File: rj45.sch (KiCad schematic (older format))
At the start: 0 parts

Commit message: Added isolators and RJ-45 connectors
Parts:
- added Jx: RJ45, symbol Connector:RJ45
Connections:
- net labels added: GNDREF, OUT1, OUT2, OUT3, OUT4
- wire segments 0 -> 12
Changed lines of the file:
@@
 $Descr A4 11693 8268
 encoding utf-8
-Sheet 5 5
+Sheet 8 8
 Title ""
 Date ""
@@
 Comment4 ""
 $EndDescr
+$Comp
+L Connector:RJ45 Jx
+U 1 1 5BCCA258
+P 6050 4100
+F 0 "Jx" H 5720 4196 50  0000 R CNN
+F 1 "RJ45" H 5720 4105 50  0000 R CNN
+F 2 "" V 6050 4125 50  0001 C CNN
+F 3 "~" V 6050 4125 50  0001 C CNN
+	1    6050 4100
+	-1   0    0    -1
+$EndComp
+$Comp
+L power:GNDREF #PWR?
+U 1 1 5BCCA2D6
+P 5450 4600
+F 0 "#PWR?" H 5450 4350 50  0001 C CNN
+F 1 "GNDREF" H 5455 4427 50  0000 C CNN
+F 2 "" H 5450 4600 50  0001 C CNN
+F 3 "" H 5450 4600 50  0001 C CNN
+	1    5450 4600
+	1    0    0    -1
+$EndComp
+Wire Wire Line
+	5450 4600 5450 4400
+Wire Wire Line
+	5450 3800 5650 3800
+Wire Wire Line
+	5650 4000 5450 4000
+Connection ~ 5450 4000
+Wire Wire Line
+	5450 4000 5450 3800
+Wire Wire Line
+	5650 4200 5450 4200
+Connection ~ 5450 4200
+Wire Wire Line
+	5450 4200 5450 4000
+Wire Wire Line
+	5650 4400 5450 4400
+Connection ~ 5450 4400
+Wire Wire Line
+	5450 4400 5450 4200
+Text HLabel 5200 3700 0    50   Input ~ 0
+OUT1
+Text HLabel 5200 3900 0    50   Input ~ 0
+OUT2
+Text HLabel 5200 4100 0    50   Input ~ 0
+OUT3
+Text HLabel 5200 4300 0    50   Input ~ 0
+OUT4
+Wire Wire Line
+	5200 4300 5650 4300
+Wire Wire Line
+	5200 4100 5650 4100
+Wire Wire Line
+	5200 3900 5650 3900
+Wire Wire Line
+	5200 3700 5650 3700
 $EndSCHEMATC

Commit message: Added charge pump IC REG71050
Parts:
- renumbered Jx to Jx1
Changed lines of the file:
@@
 $Descr A4 11693 8268
 encoding utf-8
-Sheet 8 8
+Sheet 8 11
 Title ""
 Date ""
@@
 $EndDescr
 $Comp
-L Connector:RJ45 Jx
+L Connector:RJ45 Jx1
 U 1 1 5BCCA258
 P 6050 4100
-F 0 "Jx" H 5720 4196 50  0000 R CNN
+AR Path="/5BCCA241/5BCCA258" Ref="Jx1"  Part="1"
+AR Path="/5BCCB065/5BCCA258" Ref="Jx2"  Part="1"
+AR Path="/5BCCB3D0/5BCCA258" Ref="Jx3"  Part="1"
+AR Path="/5BCCB87F/5BCCA258" Ref="Jx4"  Part="1"
+F 0 "Jx1" H 5720 4196 50  0000 R CNN
 F 1 "RJ45" H 5720 4105 50  0000 R CNN
 F 2 "" V 6050 4125 50  0001 C CNN
@@
 $EndComp
 $Comp
-L power:GNDREF #PWR?
+L power:GNDREF #PWR0126
 U 1 1 5BCCA2D6
 P 5450 4600
-F 0 "#PWR?" H 5450 4350 50  0001 C CNN
+AR Path="/5BCCA241/5BCCA2D6" Ref="#PWR0126"  Part="1"
+AR Path="/5BCCB065/5BCCA2D6" Ref="#PWR0127"  Part="1"
+AR Path="/5BCCB3D0/5BCCA2D6" Ref="#PWR0128"  Part="1"
+AR Path="/5BCCB87F/5BCCA2D6" Ref="#PWR0129"  Part="1"
+F 0 "#PWR0126" H 5450 4350 50  0001 C CNN
 F 1 "GNDREF" H 5455 4427 50  0000 C CNN
 F 2 "" H 5450 4600 50  0001 C CNN

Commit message: Assigned footprints
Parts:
- Jx1: footprint (none) -> Connector_RJ:RJ45_Amphenol_54602-x08_Horizontal
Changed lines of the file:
@@
 F 0 "Jx1" H 5720 4196 50  0000 R CNN
 F 1 "RJ45" H 5720 4105 50  0000 R CNN
-F 2 "" V 6050 4125 50  0001 C CNN
+F 2 "Connector_RJ:RJ45_Amphenol_54602-x08_Horizontal" V 6050 4125 50  0001 C CNN
 F 3 "~" V 6050 4125 50  0001 C CNN
 	1    6050 4100

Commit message: Continued layouting
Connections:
- net labels added: GND
- net labels removed: GNDREF
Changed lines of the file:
@@
 AR Path="/5BCCB3D0/5BCCA258" Ref="Jx3"  Part="1"
 AR Path="/5BCCB87F/5BCCA258" Ref="Jx4"  Part="1"
-F 0 "Jx1" H 5720 4196 50  0000 R CNN
+F 0 "Jx4" H 5720 4196 50  0000 R CNN
 F 1 "RJ45" H 5720 4105 50  0000 R CNN
 F 2 "Connector_RJ:RJ45_Amphenol_54602-x08_Horizontal" V 6050 4125 50  0001 C CNN
@@
 	1    6050 4100
 	-1   0    0    -1
-$EndComp
-$Comp
-L power:GNDREF #PWR0126
-U 1 1 5BCCA2D6
-P 5450 4600
-AR Path="/5BCCA241/5BCCA2D6" Ref="#PWR0126"  Part="1"
-AR Path="/5BCCB065/5BCCA2D6" Ref="#PWR0127"  Part="1"
-AR Path="/5BCCB3D0/5BCCA2D6" Ref="#PWR0128"  Part="1"
-AR Path="/5BCCB87F/5BCCA2D6" Ref="#PWR0129"  Part="1"
-F 0 "#PWR0126" H 5450 4350 50  0001 C CNN
-F 1 "GNDREF" H 5455 4427 50  0000 C CNN
-F 2 "" H 5450 4600 50  0001 C CNN
-F 3 "" H 5450 4600 50  0001 C CNN
-	1    5450 4600
-	1    0    0    -1
 $EndComp
 Wire Wire Line
@@
 Wire Wire Line
 	5200 3700 5650 3700
+$Comp
+L power:GND #PWR042
+U 1 1 5BCF77E9
+P 5450 4600
+AR Path="/5BCCA241/5BCF77E9" Ref="#PWR042"  Part="1"
+AR Path="/5BCCB065/5BCF77E9" Ref="#PWR043"  Part="1"
+AR Path="/5BCCB3D0/5BCF77E9" Ref="#PWR044"  Part="1"
+AR Path="/5BCCB87F/5BCF77E9" Ref="#PWR045"  Part="1"
+F 0 "#PWR045" H 5450 4350 50  0001 C CNN
+F 1 "GND" H 5455 4427 50  0000 C CNN
+F 2 "" H 5450 4600 50  0001 C CNN
+F 3 "" H 5450 4600 50  0001 C CNN
+	1    5450 4600
+	1    0    0    -1
+$EndComp
 $EndSCHEMATC

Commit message: Switched to Si8660 isolator and changed RJ-45 connector
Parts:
- removed Jx1: RJ45, Connector_RJ:RJ45_Amphenol_54602-x08_Horizontal, symbol Connector:RJ45
- added J3: TE-Connectivity-406549-6, Matthias:TE-Connectivity-406549-6, symbol Matthias:TE-Connectivity-406549-6
- added R1, R2: R_Small, symbol Device:R_Small
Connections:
- net labels added: LED1, LED2
- wire segments 12 -> 23
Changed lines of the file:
@@
 $Descr A4 11693 8268
 encoding utf-8
-Sheet 8 11
+Sheet 10 11
 Title ""
 Date ""
@@
 Comment4 ""
 $EndDescr
+Wire Wire Line
+	6900 3800 6700 3800
+Wire Wire Line
+	6700 4000 6900 4000
+Connection ~ 6900 4000
+Wire Wire Line
+	6900 4000 6900 3800
+Wire Wire Line
+	6700 4200 6900 4200
+Connection ~ 6900 4200
+Wire Wire Line
+	6900 4200 6900 4000
+Wire Wire Line
+	6700 4400 6900 4400
+Connection ~ 6900 4400
+Wire Wire Line
+	6900 4400 6900 4200
+Text HLabel 7150 3700 2    50   Input ~ 0
+OUT1
+Text HLabel 7150 3900 2    50   Input ~ 0
+OUT2
+Text HLabel 7150 4100 2    50   Input ~ 0
+OUT3
+Text HLabel 7150 4300 2    50   Input ~ 0
+OUT4
+Wire Wire Line
+	7150 4300 6700 4300
+Wire Wire Line
+	7150 4100 6700 4100
+Wire Wire Line
+	7150 3900 6700 3900
+Wire Wire Line
+	7150 3700 6700 3700
 $Comp
-L Connector:RJ45 Jx1
-U 1 1 5BCCA258
-P 6050 4100
-AR Path="/5BCCA241/5BCCA258" Ref="Jx1"  Part="1"
-AR Path="/5BCCB065/5BCCA258" Ref="Jx2"  Part="1"
-AR Path="/5BCCB3D0/5BCCA258" Ref="Jx3"  Part="1"
-AR Path="/5BCCB87F/5BCCA258" Ref="Jx4"  Part="1"
-F 0 "Jx4" H 5720 4196 50  0000 R CNN
-F 1 "RJ45" H 5720 4105 50  0000 R CNN
-F 2 "Connector_RJ:RJ45_Amphenol_54602-x08_Horizontal" V 6050 4125 50  0001 C CNN
-F 3 "~" V 6050 4125 50  0001 C CNN
-	1    6050 4100
-	-1   0    0    -1
+L power:GND #PWR044
+U 1 1 5BCF77E9
+P 6900 4950
+AR Path="/5BCCA241/5BCF77E9" Ref="#PWR044"  Part="1"
+AR Path="/5BCCB065/5BCF77E9" Ref="#PWR047"  Part="1"
+AR Path="/5BCCB3D0/5BCF77E9" Ref="#PWR050"  Part="1"
+AR Path="/5BCCB87F/5BCF77E9" Ref="#PWR053"  Part="1"
+F 0 "#PWR053" H 6900 4700 50  0001 C CNN
+F 1 "GND" H 6905 4777 50  0000 C CNN
+F 2 "" H 6900 4950 50  0001 C CNN
+F 3 "" H 6900 4950 50  0001 C CNN
+	1    6900 4950
+	1    0    0    -1
+$EndComp
+$Comp
+L Matthias:TE-Connectivity-406549-6 J3
+U 1 1 5BE0C1CD
+P 6300 4100
+AR Path="/5BCCA241/5BE0C1CD" Ref="J3"  Part="1"
+AR Path="/5BCCB3D0/5BE0C1CD" Ref="J5"  Part="1"
+AR Path="/5BCCB065/5BE0C1CD" Ref="J4"  Part="1"
+AR Path="/5BCCB87F/5BE0C1CD" Ref="J6"  Part="1"
+F 0 "J6" H 6300 4775 50  0000 C CNN
+F 1 "TE-Connectivity-406549-6" H 6300 4684 50  0000 C CNN
+F 2 "Matthias:TE-Connectivity-406549-6" V 6300 4125 50  0001 C CNN
+F 3 "~" V 6300 4125 50  0001 C CNN
+	1    6300 4100
+	1    0    0    -1
+$EndComp
+Text HLabel 5550 3750 0    50   Input ~ 0
+LED1
+Text HLabel 5550 4450 0    50   Input ~ 0
+LED2
+Wire Wire Line
+	6900 4400 6900 4750
+Wire Wire Line
+	6250 4650 6250 4750
+Wire Wire Line
+	6250 4750 6400 4750
+Connection ~ 6900 4750
+Wire Wire Line
+	6900 4750 6900 4950
+Wire Wire Line
+	6400 4650 6400 4750
+Connection ~ 6400 4750
+Wire Wire Line
+	6400 4750 6900 4750
+Wire Wire Line
+	5900 4450 5550 4450
+Wire Wire Line
+	5900 3750 5550 3750
+$Comp
+L Device:R_Small R1
+U 1 1 5BE0DDBF
+P 5100 3650
+AR Path="/5BCCA241/5BE0DDBF" Ref="R1"  Part="1"
+AR Path="/5BCCB3D0/5BE0DDBF" Ref="R5"  Part="1"
+AR Path="/5BCCB065/5BE0DDBF" Ref="R3"  Part="1"
+AR Path="/5BCCB87F/5BE0DDBF" Ref="R7"  Part="1"
+F 0 "R7" V 4904 3650 50  0000 C CNN
+F 1 "R_Small" V 4995 3650 50  0000 C CNN
+F 2 "" H 5100 3650 50  0001 C CNN
+F 3 "~" H 5100 3650 50  0001 C CNN
+	1    5100 3650
+	0    1    1    0
 $EndComp
 Wire Wire Line
-	5450 4600 5450 4400
-Wire Wire Line
-	5450 3800 5650 3800
-Wire Wire Line
-	5650 4000 5450 4000
-Connection ~ 5450 4000
-Wire Wire Line
-	5450 4000 5450 3800
-Wire Wire Line
-	5650 4200 5450 4200
-Connection ~ 5450 4200
-Wire Wire Line
-	5450 4200 5450 4000
-Wire Wire Line
-	5650 4400 5450 4400
-Connection ~ 5450 4400
-Wire Wire Line
-	5450 4400 5450 4200
-Text HLabel 5200 3700 0    50   Input ~ 0
-OUT1
-Text HLabel 5200 3900 0    50   Input ~ 0
-OUT2
-Text HLabel 5200 4100 0    50   Input ~ 0
-OUT3
-Text HLabel 5200 4300 0    50   Input ~ 0
-OUT4
-Wire Wire Line
-	5200 4300 5650 4300
-Wire Wire Line
-	5200 4100 5650 4100
-Wire Wire Line
-	5200 3900 5650 3900
-Wire Wire Line
-	5200 3700 5650 3700
+	5200 3650 5900 3650
 $Comp
 L power:GND #PWR042
-U 1 1 5BCF77E9
-P 5450 4600
-AR Path="/5BCCA241/5BCF77E9" Ref="#PWR042"  Part="1"
-AR Path="/5BCCB065/5BCF77E9" Ref="#PWR043"  Part="1"
-AR Path="/5BCCB3D0/5BCF77E9" Ref="#PWR044"  Part="1"
-AR Path="/5BCCB87F/5BCF77E9" Ref="#PWR045"  Part="1"
-F 0 "#PWR045" H 5450 4350 50  0001 C CNN
-F 1 "GND" H 5455 4427 50  0000 C CNN
-F 2 "" H 5450 4600 50  0001 C CNN
-F 3 "" H 5450 4600 50  0001 C CNN
-	1    5450 4600
+U 1 1 5BE0E201
+P 5000 3800
+AR Path="/5BCCA241/5BE0E201" Ref="#PWR042"  Part="1"
+AR Path="/5BCCB065/5BE0E201" Ref="#PWR045"  Part="1"
+AR Path="/5BCCB3D0/5BE0E201" Ref="#PWR048"  Part="1"
+AR Path="/5BCCB87F/5BE0E201" Ref="#PWR051"  Part="1"
+F 0 "#PWR051" H 5000 3550 50  0001 C CNN
+F 1 "GND" H 5005 3627 50  0000 C CNN
+F 2 "" H 5000 3800 50  0001 C CNN
+F 3 "" H 5000 3800 50  0001 C CNN
+	1    5000 3800
 	1    0    0    -1
 $EndComp
+Wire Wire Line
+	5000 3800 5000 3650
+$Comp
+L Device:R_Small R2
+U 1 1 5BE0E685
+P 5100 4350
+AR Path="/5BCCA241/5BE0E685" Ref="R2"  Part="1"
+AR Path="/5BCCB3D0/5BE0E685" Ref="R6"  Part="1"
+AR Path="/5BCCB065/5BE0E685" Ref="R4"  Part="1"
+AR Path="/5BCCB87F/5BE0E685" Ref="R8"  Part="1"
+F 0 "R8" V 4904 4350 50  0000 C CNN
+F 1 "R_Small" V 4995 4350 50  0000 C CNN
+F 2 "" H 5100 4350 50  0001 C CNN
+F 3 "~" H 5100 4350 50  0001 C CNN
+	1    5100 4350
+	0    1    1    0
+$EndComp
+Wire Wire Line
+	5200 4350 5900 4350
+$Comp
+L power:GND #PWR043
+U 1 1 5BE0E68D
+P 5000 4500
+AR Path="/5BCCA241/5BE0E68D" Ref="#PWR043"  Part="1"
+AR Path="/5BCCB065/5BE0E68D" Ref="#PWR046"  Part="1"
+AR Path="/5BCCB3D0/5BE0E68D" Ref="#PWR049"  Part="1"
+AR Path="/5BCCB87F/5BE0E68D" Ref="#PWR052"  Part="1"
+F 0 "#PWR052" H 5000 4250 50  0001 C CNN
+F 1 "GND" H 5005 4327 50  0000 C CNN
+F 2 "" H 5000 4500 50  0001 C CNN
+F 3 "" H 5000 4500 50  0001 C CNN
+	1    5000 4500
+	1    0    0    -1
+$EndComp
+Wire Wire Line
+	5000 4500 5000 4350
 $EndSCHEMATC

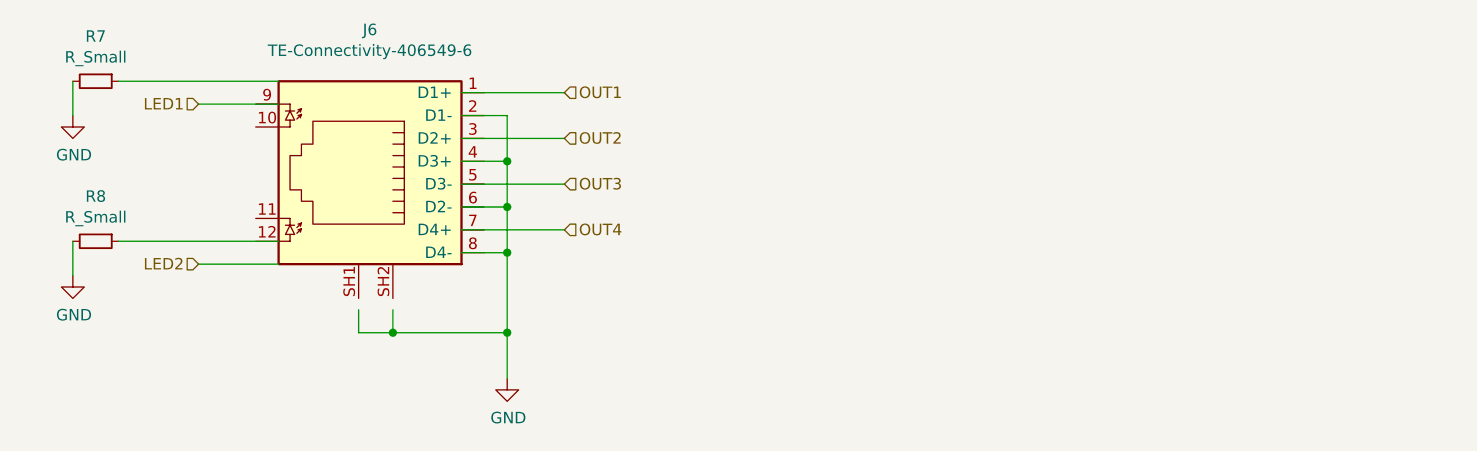
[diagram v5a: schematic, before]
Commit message: Updated RJ45 symbol and corresponding signal names
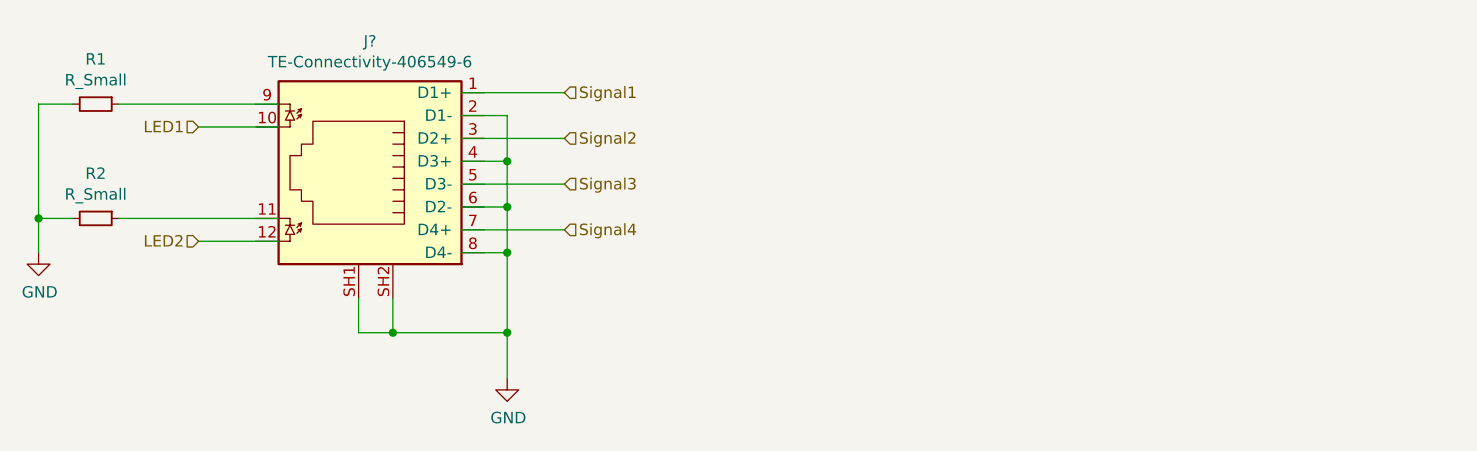
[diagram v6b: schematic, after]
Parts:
- removed J3: TE-Connectivity-406549-6, Matthias:TE-Connectivity-406549-6, symbol Matthias:TE-Connectivity-406549-6
- added J?: TE-Connectivity-406549-6, symbol Matthias:TE-Connectivity-406549-6
- R1, R2: footprint (none) -> Resistor_SMD:R_0805_2012Metric_Pad1.15x1.40mm_HandSolder
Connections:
- net labels added: Signal1, Signal2, Signal3, Signal4
- net labels removed: OUT1, OUT2, OUT3, OUT4
- wire segments 23 -> 25
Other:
- moved on the sheet: R1, R2
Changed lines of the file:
@@
 $Descr A4 11693 8268
 encoding utf-8
-Sheet 10 11
+Sheet 8 11
 Title ""
 Date ""
@@
 	6900 4400 6900 4200
 Text HLabel 7150 3700 2    50   Input ~ 0
-OUT1
+Signal1
 Text HLabel 7150 3900 2    50   Input ~ 0
-OUT2
+Signal2
 Text HLabel 7150 4100 2    50   Input ~ 0
-OUT3
+Signal3
 Text HLabel 7150 4300 2    50   Input ~ 0
-OUT4
+Signal4
 Wire Wire Line
 	7150 4300 6700 4300
@@
 AR Path="/5BCCB3D0/5BCF77E9" Ref="#PWR050"  Part="1"
 AR Path="/5BCCB87F/5BCF77E9" Ref="#PWR053"  Part="1"
-F 0 "#PWR053" H 6900 4700 50  0001 C CNN
+F 0 "#PWR044" H 6900 4700 50  0001 C CNN
 F 1 "GND" H 6905 4777 50  0000 C CNN
 F 2 "" H 6900 4950 50  0001 C CNN
@@
 	1    0    0    -1
 $EndComp
-$Comp
-L Matthias:TE-Connectivity-406549-6 J3
-U 1 1 5BE0C1CD
-P 6300 4100
-AR Path="/5BCCA241/5BE0C1CD" Ref="J3"  Part="1"
-AR Path="/5BCCB3D0/5BE0C1CD" Ref="J5"  Part="1"
-AR Path="/5BCCB065/5BE0C1CD" Ref="J4"  Part="1"
-AR Path="/5BCCB87F/5BE0C1CD" Ref="J6"  Part="1"
-F 0 "J6" H 6300 4775 50  0000 C CNN
-F 1 "TE-Connectivity-406549-6" H 6300 4684 50  0000 C CNN
-F 2 "Matthias:TE-Connectivity-406549-6" V 6300 4125 50  0001 C CNN
-F 3 "~" V 6300 4125 50  0001 C CNN
-	1    6300 4100
-	1    0    0    -1
-$EndComp
-Text HLabel 5550 3750 0    50   Input ~ 0
+Text HLabel 5550 3850 0    50   Input ~ 0
 LED1
-Text HLabel 5550 4450 0    50   Input ~ 0
+Text HLabel 5550 4350 0    50   Input ~ 0
 LED2
 Wire Wire Line
 	6900 4400 6900 4750
 Wire Wire Line
-	6250 4650 6250 4750
+	6250 4600 6250 4750
 Wire Wire Line
 	6250 4750 6400 4750
@@
 	6900 4750 6900 4950
 Wire Wire Line
-	6400 4650 6400 4750
+	6400 4600 6400 4750
 Connection ~ 6400 4750
 Wire Wire Line
 	6400 4750 6900 4750
 Wire Wire Line
-	5900 4450 5550 4450
+	5900 4350 5550 4350
 Wire Wire Line
-	5900 3750 5550 3750
+	5900 3850 5550 3850
 $Comp
 L Device:R_Small R1
 U 1 1 5BE0DDBF
-P 5100 3650
+P 5100 3750
 AR Path="/5BCCA241/5BE0DDBF" Ref="R1"  Part="1"
 AR Path="/5BCCB3D0/5BE0DDBF" Ref="R5"  Part="1"
 AR Path="/5BCCB065/5BE0DDBF" Ref="R3"  Part="1"
 AR Path="/5BCCB87F/5BE0DDBF" Ref="R7"  Part="1"
-F 0 "R7" V 4904 3650 50  0000 C CNN
-F 1 "R_Small" V 4995 3650 50  0000 C CNN
-F 2 "" H 5100 3650 50  0001 C CNN
-F 3 "~" H 5100 3650 50  0001 C CNN
-	1    5100 3650
+F 0 "R1" V 4904 3750 50  0000 C CNN
+F 1 "R_Small" V 4995 3750 50  0000 C CNN
+F 2 "Resistor_SMD:R_0805_2012Metric_Pad1.15x1.40mm_HandSolder" H 5100 3750 50  0001 C CNN
+F 3 "~" H 5100 3750 50  0001 C CNN
+	1    5100 3750
 	0    1    1    0
 $EndComp
 Wire Wire Line
-	5200 3650 5900 3650
-$Comp
-L power:GND #PWR042
-U 1 1 5BE0E201
-P 5000 3800
-AR Path="/5BCCA241/5BE0E201" Ref="#PWR042"  Part="1"
-AR Path="/5BCCB065/5BE0E201" Ref="#PWR045"  Part="1"
-AR Path="/5BCCB3D0/5BE0E201" Ref="#PWR048"  Part="1"
-AR Path="/5BCCB87F/5BE0E201" Ref="#PWR051"  Part="1"
-F 0 "#PWR051" H 5000 3550 50  0001 C CNN
-F 1 "GND" H 5005 3627 50  0000 C CNN
-F 2 "" H 5000 3800 50  0001 C CNN
-F 3 "" H 5000 3800 50  0001 C CNN
-	1    5000 3800
-	1    0    0    -1
-$EndComp
-Wire Wire Line
-	5000 3800 5000 3650
+	5200 3750 5900 3750
 $Comp
 L Device:R_Small R2
 U 1 1 5BE0E685
-P 5100 4350
+P 5100 4250
 AR Path="/5BCCA241/5BE0E685" Ref="R2"  Part="1"
 AR Path="/5BCCB3D0/5BE0E685" Ref="R6"  Part="1"
 AR Path="/5BCCB065/5BE0E685" Ref="R4"  Part="1"
 AR Path="/5BCCB87F/5BE0E685" Ref="R8"  Part="1"
-F 0 "R8" V 4904 4350 50  0000 C CNN
-F 1 "R_Small" V 4995 4350 50  0000 C CNN
-F 2 "" H 5100 4350 50  0001 C CNN
-F 3 "~" H 5100 4350 50  0001 C CNN
-	1    5100 4350
+F 0 "R2" V 4904 4250 50  0000 C CNN
+F 1 "R_Small" V 4995 4250 50  0000 C CNN
+F 2 "Resistor_SMD:R_0805_2012Metric_Pad1.15x1.40mm_HandSolder" H 5100 4250 50  0001 C CNN
+F 3 "~" H 5100 4250 50  0001 C CNN
+	1    5100 4250
 	0    1    1    0
 $EndComp
 Wire Wire Line
-	5200 4350 5900 4350
+	5200 4250 5900 4250
 $Comp
 L power:GND #PWR043
 U 1 1 5BE0E68D
-P 5000 4500
+P 4850 4400
 AR Path="/5BCCA241/5BE0E68D" Ref="#PWR043"  Part="1"
 AR Path="/5BCCB065/5BE0E68D" Ref="#PWR046"  Part="1"
 AR Path="/5BCCB3D0/5BE0E68D" Ref="#PWR049"  Part="1"
 AR Path="/5BCCB87F/5BE0E68D" Ref="#PWR052"  Part="1"
-F 0 "#PWR052" H 5000 4250 50  0001 C CNN
-F 1 "GND" H 5005 4327 50  0000 C CNN
-F 2 "" H 5000 4500 50  0001 C CNN
-F 3 "" H 5000 4500 50  0001 C CNN
-	1    5000 4500
+F 0 "#PWR043" H 4850 4150 50  0001 C CNN
+F 1 "GND" H 4855 4227 50  0000 C CNN
+F 2 "" H 4850 4400 50  0001 C CNN
+F 3 "" H 4850 4400 50  0001 C CNN
+	1    4850 4400
+	1    0    0    -1
+$EndComp
+$Comp
+L Matthias:TE-Connectivity-406549-6 J?
+U 1 1 5BE18A0E
+P 6300 4100
+F 0 "J?" H 6300 4725 50  0000 C CNN
+F 1 "TE-Connectivity-406549-6" H 6300 4634 50  0000 C CNN
+F 2 "" V 6300 4175 50  0001 C CNN
+F 3 "~" V 6300 4175 50  0001 C CNN
+	1    6300 4100
 	1    0    0    -1
 $EndComp
 Wire Wire Line
-	5000 4500 5000 4350
+	4850 3750 4850 4250
+Wire Wire Line
+	4850 3750 5000 3750
+Wire Wire Line
+	5000 4250 4850 4250
+Connection ~ 4850 4250
+Wire Wire Line
+	4850 4250 4850 4400
 $EndSCHEMATC
